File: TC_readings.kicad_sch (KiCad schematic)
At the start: 55 parts, among them J2 USB_B_Micro, J4 Conn_01x02_Pin

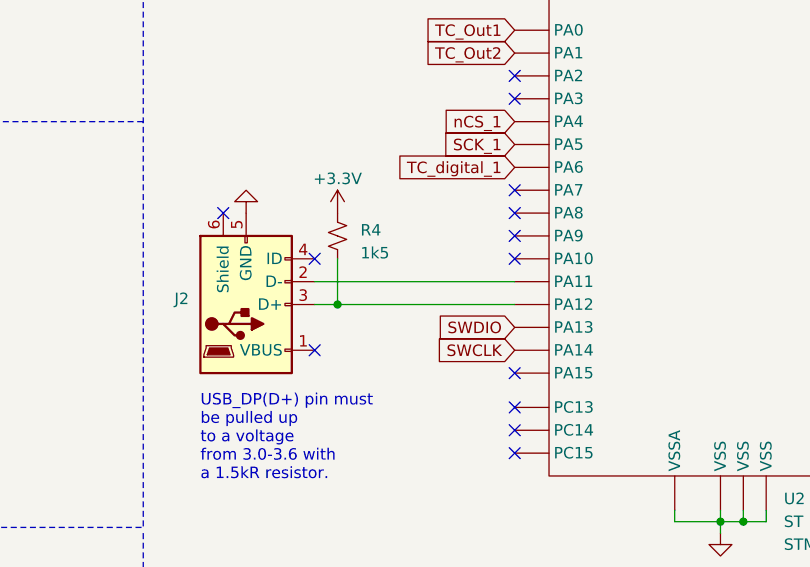
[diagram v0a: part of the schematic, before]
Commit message: Change to 4 layers
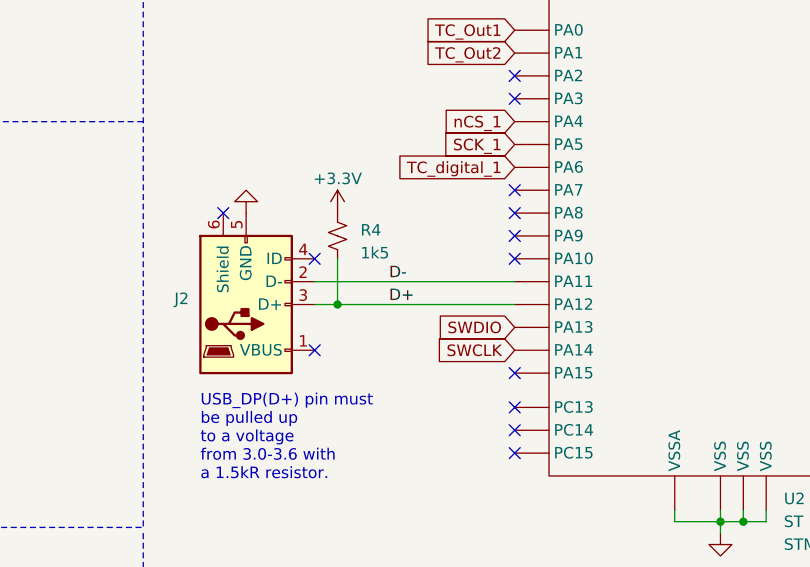
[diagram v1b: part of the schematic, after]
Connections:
- net D-: now reaches J2.2 (D-), U2.32 (PA11)
- net D+: now reaches J2.3 (D+), R4.2, U2.33 (PA12)
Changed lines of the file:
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@@
+    (effects (font (size 1.27 1.27)) (justify left bottom))
+  )
+  (label "D+" (at 202.565 80.01 0) (fields_autoplaced)
+    (effects (font (size 1.27 1.27)) (justify left bottom))
+  )
+  (label "D-" (at 202.565 77.47 0) (fields_autoplaced)
     (effects (font (size 1.27 1.27)) (justify left bottom))
   )

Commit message: Add RTD reading sensor
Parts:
- added C23, C26, C27, C28, C29: 100nF, Capacitor_SMD:C_0402_1005Metric, symbol Device:C_Small
- added R11, R12: 350, ±2ppm/°C, symbol Device:R_Small_US
- added U7, U8: ~, Package_SO:SSOP-20_5.3x7.2mm_P0.65mm, symbol UCIRP-Symbols:MAX31865
- C22: value 500nF -> 100nF
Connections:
- net +3.3V: now also C22.1, C23.1, C28.1, C29.1, U7.2 (DVDD), U7.3 (VDD), U8.2 (DVDD), U8.3 (VDD); no longer C22.2
- net GND: now also C22.2, C23.2, C28.2, C29.2, U7.13 (GND2), U7.18 (DGND), U7.19 (GND), U8.13 (GND2), U8.18 (DGND), U8.19 (GND); no longer C22.1
- new net: R11.1, U7.4 (BIAS), U7.5 (REFIN+)
- new net: R11.2, U7.6 (REFIN-), U7.7 (ISENSOR)
- new net: R12.1, U8.4 (BIAS), U8.5 (REFIN+)
- new net: R12.2, U8.6 (REFIN-), U8.7 (ISENSOR)
- new net RTD1_SDI: U7.14 (SDI)
- new net RTD1_SDO: U7.17 (SDO)
- new net RTD1_cable1: U7.8 (FORCE+), U7.9 (FORCE2)
- new net RTD1_cable2: C26.1, U7.10 (RTDIN+)
- new net RTD1_cable3: C26.2, U7.11 (RTDIN-), U7.12 (FORCE-)
- new net RTD2_SDI: U8.14 (SDI)
- new net RTD2_SDO: U8.17 (SDO)
- new net RTD2_cable1: U8.8 (FORCE+), U8.9 (FORCE2)
- new net RTD2_cable2: C27.1, U8.10 (RTDIN+)
- new net RTD2_cable3: C27.2, U8.11 (RTDIN-), U8.12 (FORCE-)
- new net SCK_3: U7.15 (SCLK)
- new net SCK_4: U8.15 (SCLK)
- new net nCS_3: U7.16 (~{CS})
- new net nCS_4: U8.16 (~{CS})
- no-connect marks 30 -> 32
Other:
- note added: "For a PT100, the datasheet recommends R_ref = 400ohm, but out of stock. Texas' guide on reading RTDs shows R_ref = 350ohm gives readings in the smaller range -200 to 650 °C, ok for us."
- note added: "MAX31865 RTD1"
- note added: "MAX31865 RTD2"
- moved on the sheet: C11, C13, C15, C16, C3, C4, C5, C6, C7, D2, J2, J4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
